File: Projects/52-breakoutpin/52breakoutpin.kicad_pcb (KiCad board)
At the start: 2 copper layers, 76.2 x 153.7 mm, 5 parts, among them J1 172319-1, J2 Conn_01x40, J3 Screw_Terminal_01x03, J4 Screw_Terminal_01x02

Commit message: PCB and Schematics edit
Made changes to both the schematic and PCB layout
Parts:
- D1: value D_Zener -> 1N4732A
- J2: footprint Connector_PinHeader_2.54mm:PinHeader_2x20_P2.54mm_Horizontal -> Connector_IDC:IDC-Header_2x20_P2.54mm_Vertical
- moved D1 100.4 mm to (109.2, 53.3), turned to 270 degrees
- moved J4 95.7 mm to (109.2, 77.5), turned to 180 degrees
- moved J3 22.7 mm to (114.3, 48.3)
- moved J2 19.8 mm to (105.4, 88.9)
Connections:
- net Net-(J1-Pad18) renamed Knock
- net Net-(J2-Pad15) renamed Fan
- net Net-(J2-Pad17) renamed Tacho
- net Net-(J2-Pad24) renamed Cam
- net Net-(J2-Pad25) renamed Crank
- J1 pad 42: Net-(J1-Pad42) -> Earth
- J1 pad 43: Net-(J1-Pad43) -> Earth
- J2 pad 14: Clutch-in -> Net-(J2-Pad14)
- J2 pad 18: Net-(J2-Pad18) -> Clutch-in
- J2 pad 21: Net-(J2-Pad21) -> O2
- J3 pad 3: IAT -> TPS
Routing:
- net 5V: track 0.00 -> 139.4 mm
- net Earth: track 0.00 -> 124.4 mm
- net 12V: track 0.00 -> 122.2 mm
- net IAT: track 0.00 -> 118.1 mm
- net TPS: track 0.00 -> 116.4 mm
- net INj2: track 0.00 -> 114.4 mm
- net Idle: track 0.00 -> 99.9 mm
- net INj3: track 0.00 -> 98.4 mm
- net INj1: track 0.00 -> 96.8 mm
- net INj4: track 0.00 -> 92.1 mm
- net Clutch-in: track 0.00 -> 58.3 mm
- net O2: track 0.00 -> 34.5 mm
- net Coolant: track 0.00 -> 31.5 mm
- net IGN1: track 0.00 -> 31.3 mm

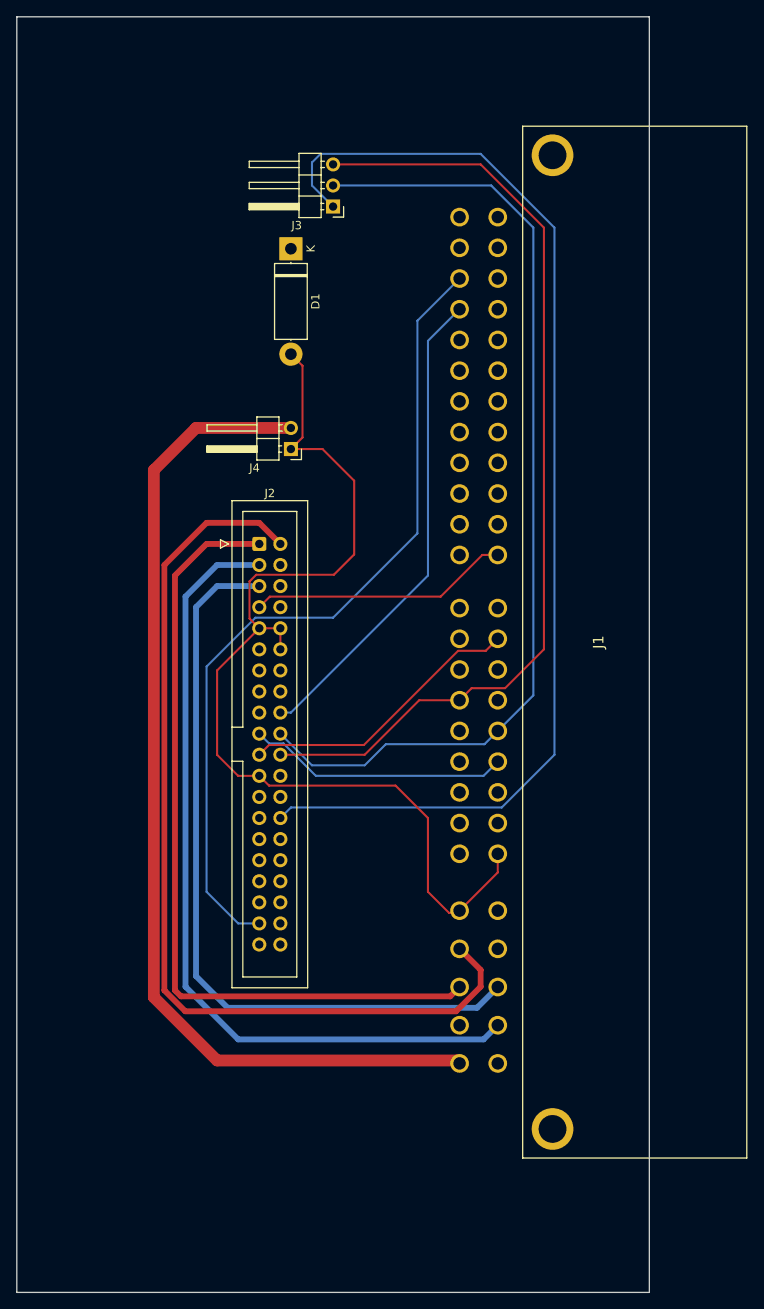
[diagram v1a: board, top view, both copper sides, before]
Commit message: Added the Cam and Crank Sensor
Connected the distributor cam and crank sensors as updated the silk screen to include branding.
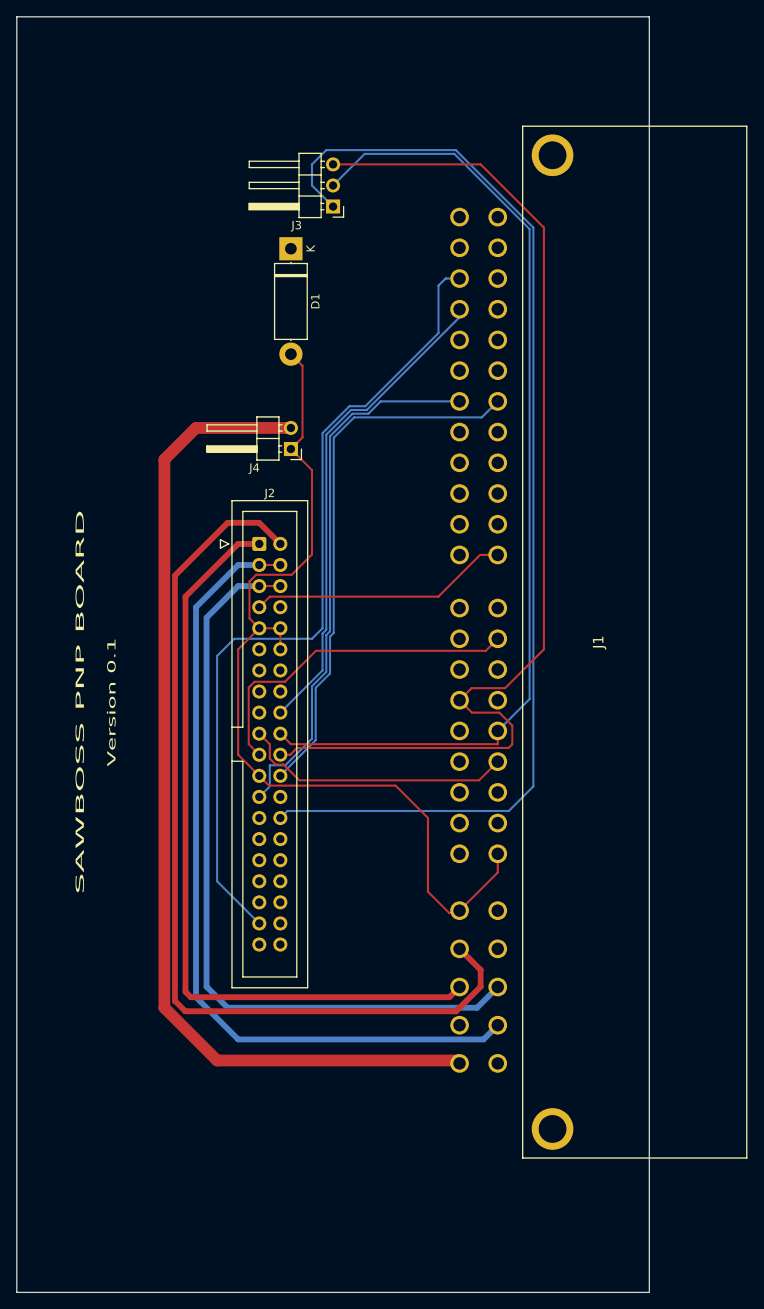
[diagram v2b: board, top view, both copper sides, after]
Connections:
- J1 pad 13: Net-(J1-Pad13) -> Crank
- J1 pad 14: Net-(J1-Pad14) -> Cam
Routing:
- net Crank: track 0.00 -> 65.4 mm
- net Cam: track 0.00 -> 65.0 mm
- net TPS: track 116.4 -> 130.4 mm
- net Earth: track 124.4 -> 111.3 mm
- net O2: track 34.5 -> 41.1 mm
- net INj1: track 96.8 -> 92.9 mm
- net 5V: track 139.4 -> 136.8 mm
- net INj2: track 114.4 -> 111.8 mm
- net Coolant: track 31.5 -> 33.0 mm
- net IAT: track 118.1 -> 119.4 mm
- net 12V: track 122.2 -> 121.2 mm
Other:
- board text added: "SAWBOSS PNP BOARD"
- board text added: "Version 0.1"
